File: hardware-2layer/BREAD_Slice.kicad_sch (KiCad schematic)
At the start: 22 parts, among them J1 Conn_01x10_Female, J2 Screw_Terminal_01x02, J3 Screw_Terminal_01x02, J4 Screw_Terminal_01x02, J5 Screw_Terminal_01x02, U2 ACS723xMATR-10AB, U3 ACS723xMATR-10AB, U4 ACS723xMATR-10AB, U5 ACS723xMATR-10AB

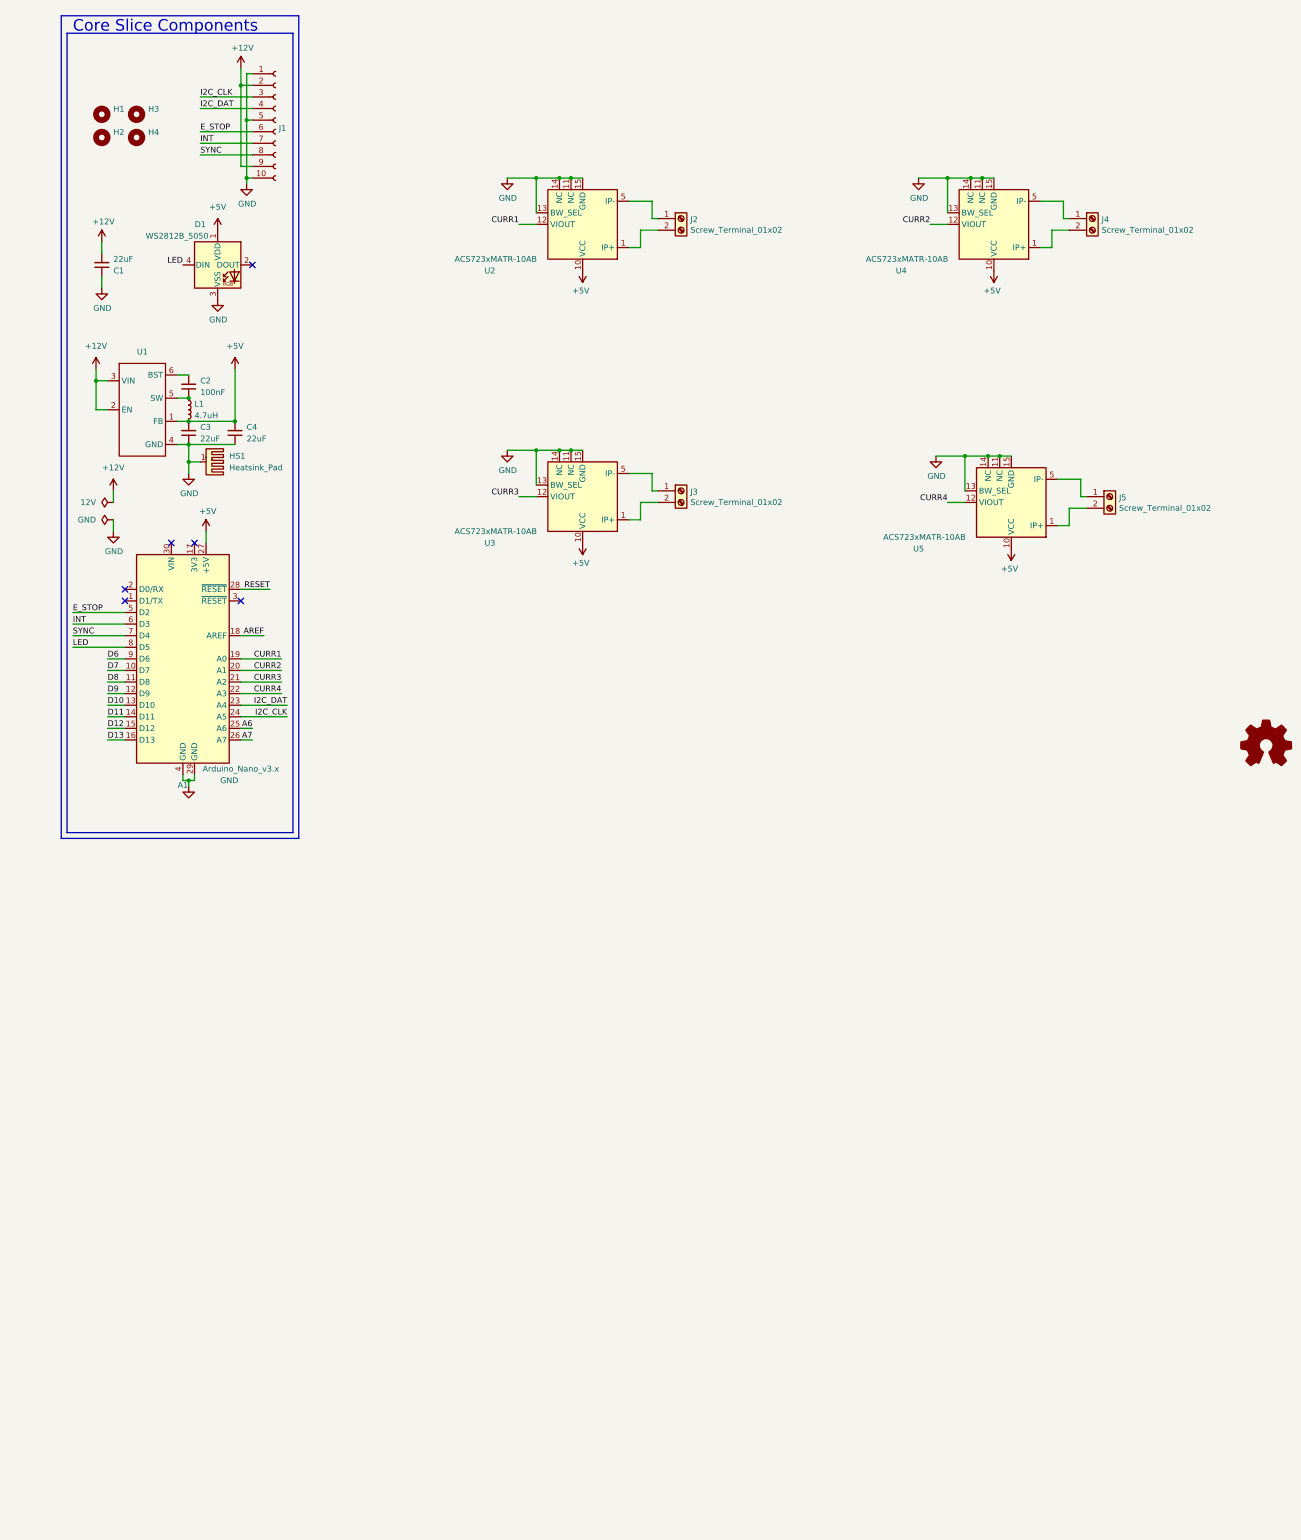
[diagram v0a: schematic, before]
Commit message: added updated CRXX and schem for CRVS iteration
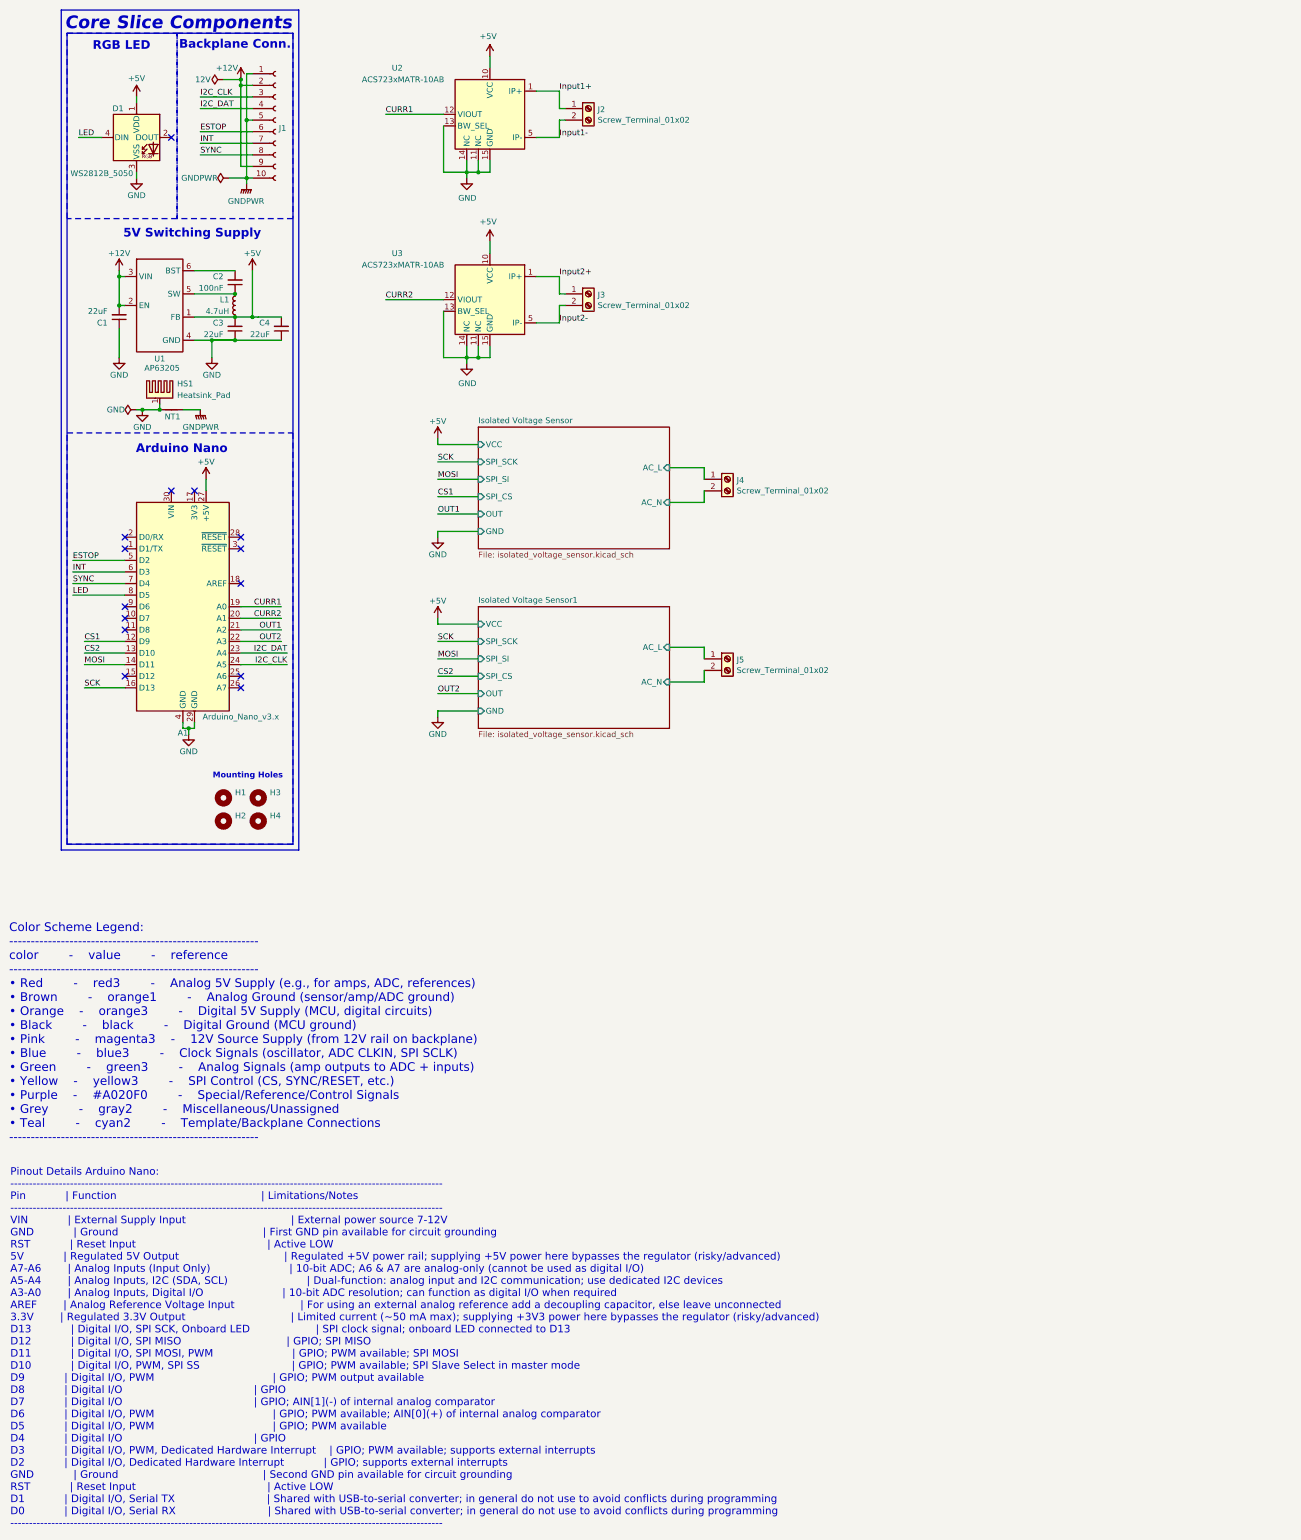
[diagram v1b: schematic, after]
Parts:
- removed U4, U5: ACS723xMATR-10AB, Package_SO:SOIC-16W_7.5x10.3mm_P1.27mm, symbol Sensor_Current:ACS723xMATR-10AB
- added NT1: NetTie_2, NetTie:NetTie-2_SMD_Pad2.0mm, symbol Device:NetTie_2
- D1: PROD_ID (none) -> DIO-12503
- HS1: footprint KML-Custom:Thermal Pad -> kml-custom:Thermal Pad
- U1: value ~ -> AP63205
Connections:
- net CURR2: now also U3.12 (VIOUT)
- net GND: now also NT1.1; no longer J1.1 (Pin_1), J1.10 (Pin_10), J1.5 (Pin_5)
- net Isolated Voltage Sensor1/AC_L: now reaches J5.1 (Pin_1)
- net Isolated Voltage Sensor1/AC_N: now reaches J5.2 (Pin_2)
- net Input1-: now reaches U2.5 (IP-), U2.6 (IP-), U2.7 (IP-), U2.8 (IP-)
- net Input1-: now also J2.2 (Pin_2); no longer J2.1 (Pin_1)
- net Input1+: now reaches U2.1 (IP+), U2.2 (IP+), U2.3 (IP+), U2.4 (IP+)
- net Input1+: now also J2.1 (Pin_1); no longer J2.2 (Pin_2)
- net Input2-: now reaches U3.5 (IP-), U3.6 (IP-), U3.7 (IP-), U3.8 (IP-)
- net Input2-: now also J3.2 (Pin_2); no longer J3.1 (Pin_1)
- net Input2+: now reaches U3.1 (IP+), U3.2 (IP+), U3.3 (IP+), U3.4 (IP+)
- net Input2+: now also J3.1 (Pin_1); no longer J3.2 (Pin_2)
- net Isolated Voltage Sensor/AC_N: now reaches J4.2 (Pin_2)
- net Isolated Voltage Sensor/AC_L: now reaches J4.1 (Pin_1)
- net A6: no longer names the net of A1.25 (A6)
- net A7: no longer names the net of A1.26 (A7)
- net AREF: no longer names the net of A1.18 (AREF)
- net CURR3 renamed OUT1
- net OUT1: no longer U3.12 (VIOUT)
- net CURR4 renamed OUT2
- net D10 renamed CS2
- net D11 renamed MOSI
- net D12: no longer names the net of A1.15 (D12)
- net D13 renamed SCK
- net D6: no longer names the net of A1.9 (D6)
- net D7: no longer names the net of A1.10 (D7)
- net D8: no longer names the net of A1.11 (D8)
- net D9 renamed CS1
- net E_STOP renamed ESTOP
- net RESET: no longer names the net of A1.28 (~{RESET})
- new net GNDPWR: J1.1 (Pin_1), J1.10 (Pin_10), J1.5 (Pin_5), NT1.2
- no-connect marks 6 -> 14
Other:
- added sheet Isolated Voltage Sensor (isolated_voltage_sensor.kicad_sch)
- added sheet Isolated Voltage Sensor1 (isolated_voltage_sensor.kicad_sch)
- note added: "5V Switching Supply"
- note added: "Arduino Nano"
- note added: "Backplane Conn."
- note added: "Color Scheme Legend: ---------------------------------------------------------- color - value - reference ---------------------------------------------------------- • Red - red3 - Analog 5V Supply (e.g., for amps, ADC, references) • Brown - orange1 - Analog Ground (sensor/amp/ADC ground) • Orange - orange3 - Digital 5V Supply (MCU, digital circuits) • Black - black - Digital Ground (MCU ground) •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"
- note added: "Mounting Holes"
- note added: "Pinout Details Arduino Nano: -------------------------------------------------------------------------------------------------------------------- Pin | Function | Limitations/Notes -------------------------------------------------------------------------------------------------------------------- VIN | External Supply Input | External power source 7-12V GND | Ground | First GND pin available for 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"
- note added: "RGB LED"
- moved on the sheet: A1, C1, C2, C3, C4, H1, H2, H3, H4, J2, J3, L1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

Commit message: final schematic done before split to ac dc
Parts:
- removed U2, U3: ACS723xMATR-10AB, Package_SO:SOIC-16W_7.5x10.3mm_P1.27mm, symbol Sensor_Current:ACS723xMATR-10AB
- added J8, J9: Screw_Terminal_01x02, CRx:Pheonix Conn Term TDPT 4 2-SP-6,35-ZB, symbol Connector:Screw_Terminal_01x02
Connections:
- net CS1: now also A1.10 (D7); no longer A1.12 (D9)
- net CS2: now also A1.11 (D8); no longer A1.13 (D10)
- net CURR1: now also A1.25 (A6); no longer A1.19 (A0)
- net CURR2: now also A1.26 (A7); no longer A1.20 (A1)
- net Input1+ renamed Invasive Isolated AC-DC Current Sensor1/IC_CS_Input+
- net Input1- renamed Invasive Isolated AC-DC Current Sensor1/IC_CS_Input-
- net Input2+ renamed Invasive Isolated AC-DC Current Sensor2/IC_CS_Input+
- net Input2- renamed Invasive Isolated AC-DC Current Sensor2/IC_CS_Input-
- net Isolated Voltage Sensor1/AC_L renamed Isolated AC Voltage Sensor2/AC_L
- net Isolated Voltage Sensor1/AC_N renamed Isolated AC Voltage Sensor2/AC_N
- net OUT1 renamed VOLT1
- net OUT2 renamed VOLT2
- new net CS3: A1.12 (D9)
- new net CS4: A1.13 (D10)
- new net IC_CURR1: A1.19 (A0)
- new net IC_CURR2: A1.20 (A1)
- new net Isolated DC Voltage Sensor1/DC_BUS+: J8.1 (Pin_1)
- new net Isolated DC Voltage Sensor1/DC_BUS-: J8.2 (Pin_2)
- new net Isolated DC Voltage Sensor2/DC_BUS+: J9.1 (Pin_1)
- new net Isolated DC Voltage Sensor2/DC_BUS-: J9.2 (Pin_2)
- no-connect marks 14 -> 10
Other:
- sheet Isolated Voltage Sensor renamed Isolated AC Voltage Sensor1
- removed sheet Isolated Voltage Sensor1
- added sheet Invasive Isolated AC-DC Current Sensor1 (isolated_acdc_current_sensor_acs724.kicad_sch)
- added sheet Invasive Isolated AC-DC Current Sensor2 (isolated_acdc_current_sensor_acs724.kicad_sch)
- added sheet Isolated AC Voltage Sensor2 (isolated_ac_voltage_sensor.kicad_sch)
- added sheet Isolated DC Voltage Sensor1 (isolated_dc_voltage_sensor.kicad_sch)
- added sheet Isolated DC Voltage Sensor2 (isolated_dc_voltage_sensor.kicad_sch)
- added sheet Non-Invasive AC Current Sensor1 (noninvasive_ac_current_sensor.kicad_sch)
- added sheet Non-Invasive AC Current Sensor2 (noninvasive_ac_current_sensor.kicad_sch)
- sheet Isolated AC Voltage Sensor1: file isolated_voltage_sensor.kicad_sch -> isolated_ac_voltage_sensor.kicad_sch
- moved on the sheet: J2, J4, J5
